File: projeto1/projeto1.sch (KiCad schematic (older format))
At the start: 17 parts

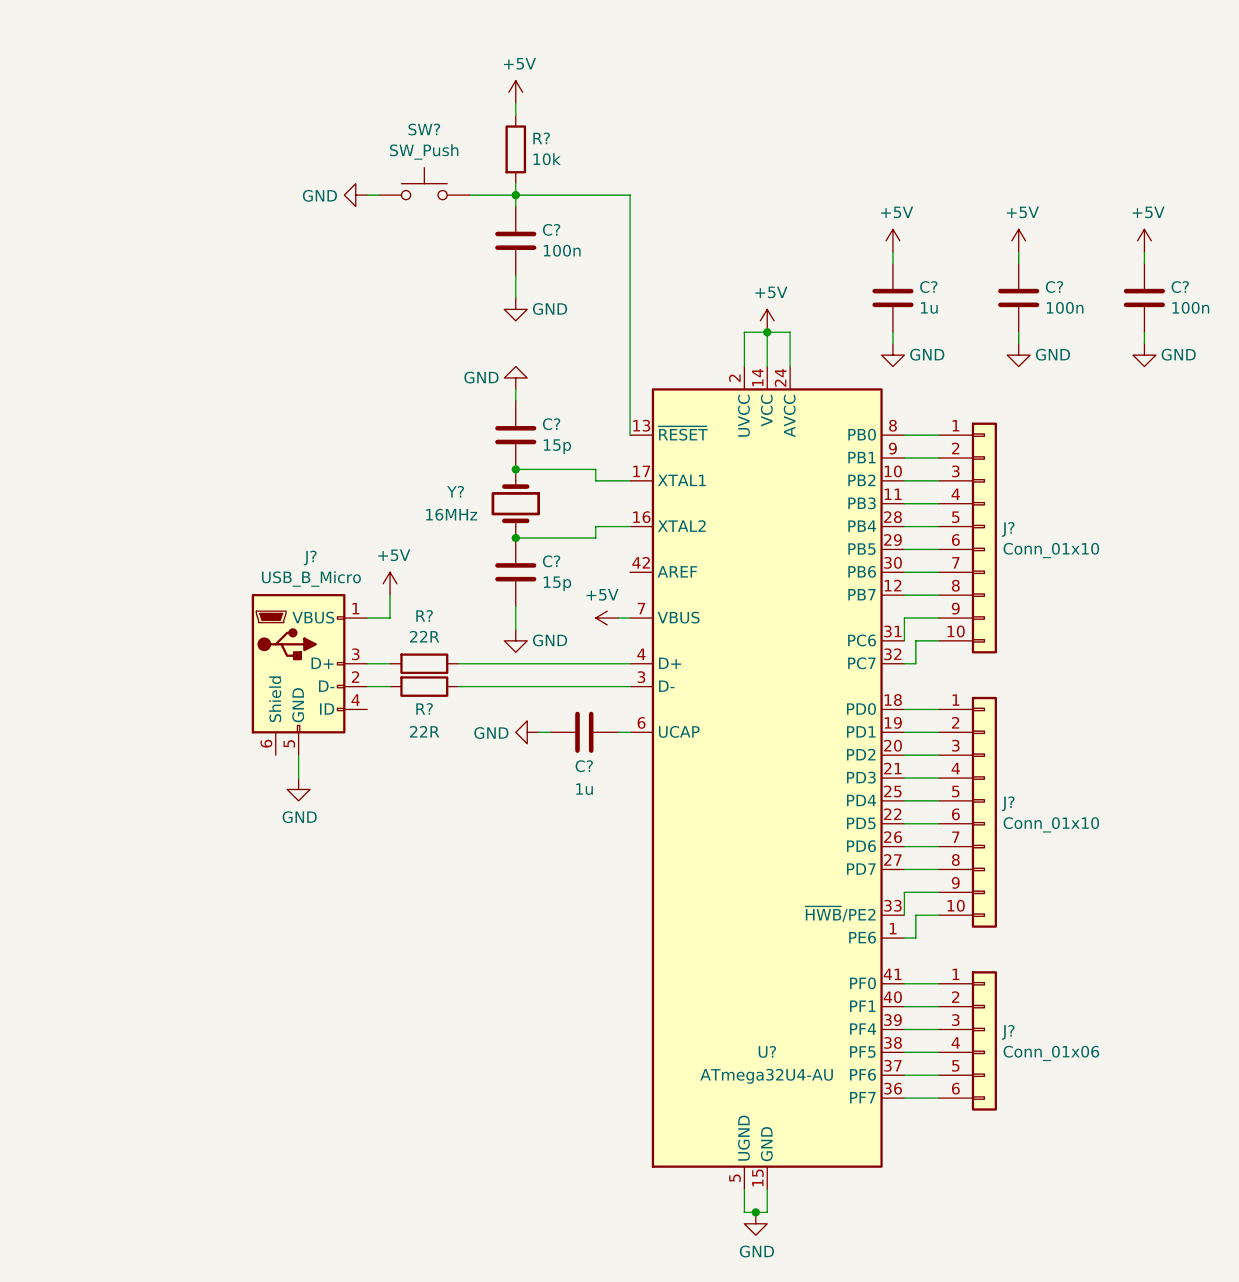
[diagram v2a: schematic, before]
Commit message: Identificadores adicionados
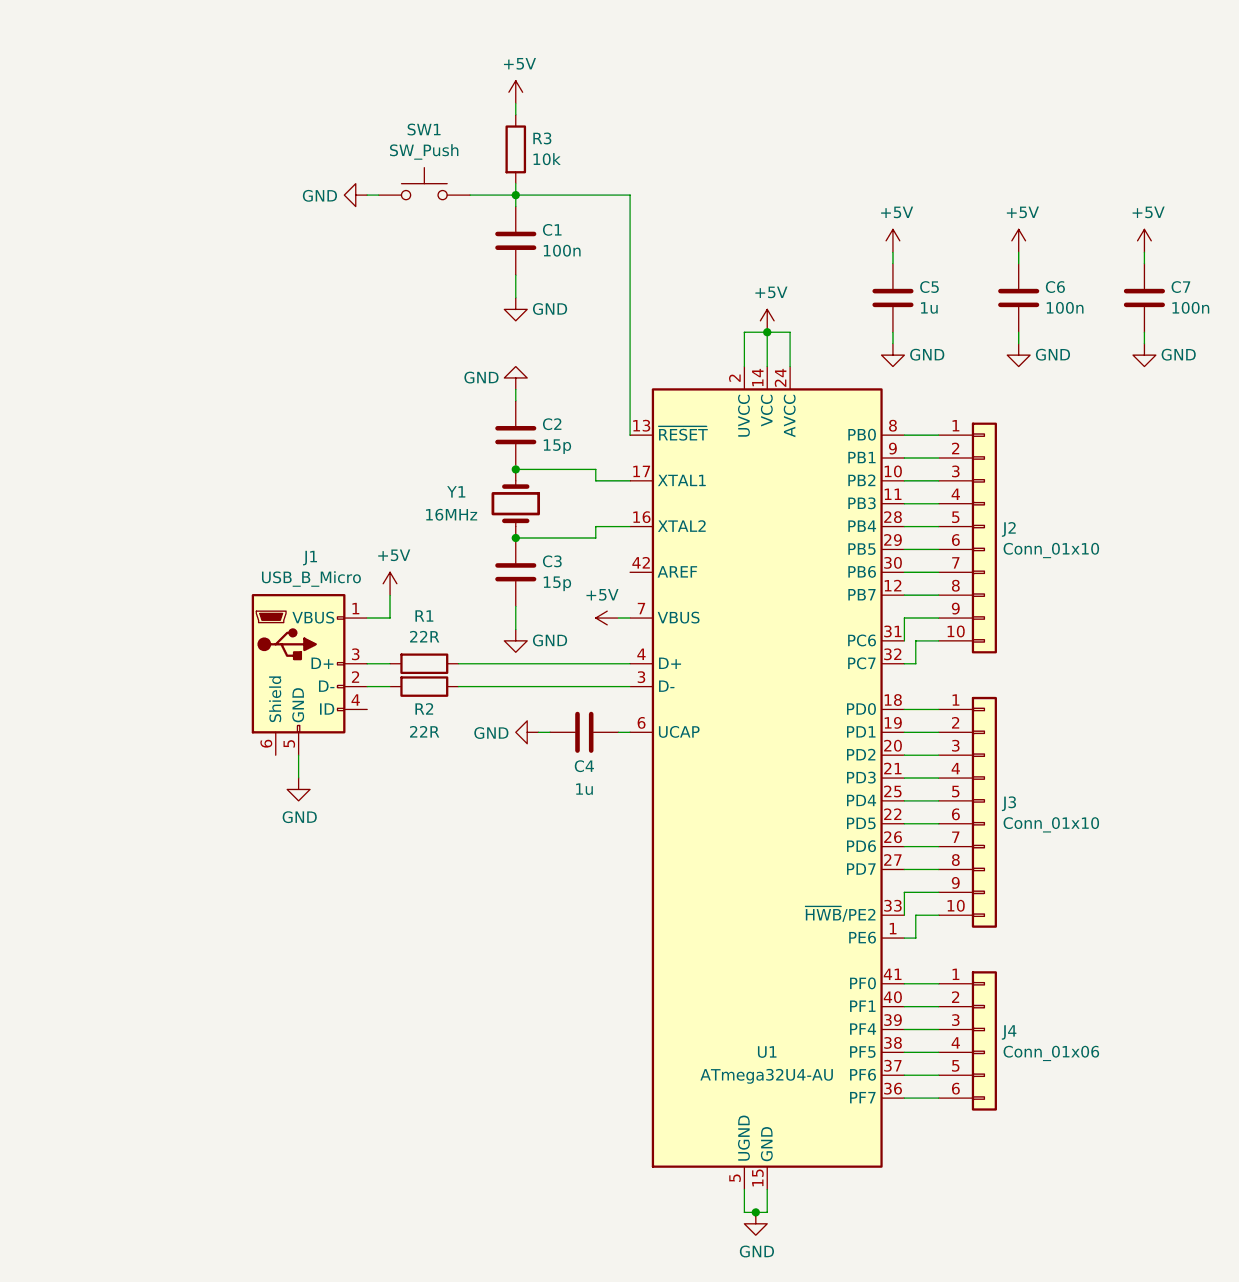
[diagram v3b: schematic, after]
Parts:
- gave numbers to parts that had none: 17
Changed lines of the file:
@@
 $EndDescr
 $Comp
-L Connector:USB_B_Micro J?
+L Connector:USB_B_Micro J1
 U 1 1 5D7A3DE3
 P 3500 3600
-F 0 "J?" H 3555 4067 50  0000 C CNN
+F 0 "J1" H 3555 4067 50  0000 C CNN
 F 1 "USB_B_Micro" H 3555 3976 50  0000 C CNN
 F 2 "" H 3650 3550 50  0001 C CNN
@@
 $EndComp
 $Comp
-L power:+5V #PWR?
+L power:+5V #PWR03
 U 1 1 5D7A3EE1
 P 3900 3300
-F 0 "#PWR?" H 3900 3150 50  0001 C CNN
+F 0 "#PWR03" H 3900 3150 50  0001 C CNN
 F 1 "+5V" H 3915 3473 50  0000 C CNN
 F 2 "" H 3900 3300 50  0001 C CNN
@@
 $EndComp
 $Comp
-L Device:R R?
+L Device:R R1
 U 1 1 5D7A400D
 P 4050 3600
-F 0 "R?" V 3843 3600 50  0000 C CNN
+F 0 "R1" V 3843 3600 50  0000 C CNN
 F 1 "22R" V 3934 3600 50  0000 C CNN
 F 2 "" V 3980 3600 50  0001 C CNN
@@
 $EndComp
 $Comp
-L Device:R R?
+L Device:R R2
 U 1 1 5D7A4271
 P 4050 3700
-F 0 "R?" V 4150 3700 50  0000 C CNN
+F 0 "R2" V 4150 3700 50  0000 C CNN
 F 1 "22R" V 4250 3700 50  0000 C CNN
 F 2 "" V 3980 3700 50  0001 C CNN
@@
 	3800 3700 3900 3700
 $Comp
-L power:GND #PWR?
+L power:GND #PWR01
 U 1 1 5D7A4CB3
 P 3500 4100
-F 0 "#PWR?" H 3500 3850 50  0001 C CNN
+F 0 "#PWR01" H 3500 3850 50  0001 C CNN
 F 1 "GND" H 3505 3927 50  0000 C CNN
 F 2 "" H 3500 4100 50  0001 C CNN
@@
 	3500 4100 3500 4000
 $Comp
-L power:+5V #PWR?
+L power:+5V #PWR011
 U 1 1 5D7A4E99
 P 5550 2150
-F 0 "#PWR?" H 5550 2000 50  0001 C CNN
+F 0 "#PWR011" H 5550 2000 50  0001 C CNN
 F 1 "+5V" H 5565 2323 50  0000 C CNN
 F 2 "" H 5550 2150 50  0001 C CNN
@@
 	5650 2150 5550 2150
 $Comp
-L power:GND #PWR?
+L power:GND #PWR010
 U 1 1 5D7A4FE0
 P 5500 6000
-F 0 "#PWR?" H 5500 5750 50  0001 C CNN
+F 0 "#PWR010" H 5500 5750 50  0001 C CNN
 F 1 "GND" H 5505 5827 50  0000 C CNN
 F 2 "" H 5500 6000 50  0001 C CNN
@@
 Connection ~ 5500 6000
 $Comp
-L Device:Crystal Y?
+L Device:Crystal Y1
 U 1 1 5D7A541D
 P 4450 2900
-F 0 "Y?" V 4400 2600 50  0000 L CNN
+F 0 "Y1" V 4400 2600 50  0000 L CNN
 F 1 "16MHz" V 4500 2500 50  0000 L CNN
 F 2 "" H 4450 2900 50  0001 C CNN
@@
 	4800 3000 4800 3050
 $Comp
-L Device:C C?
+L Device:C C2
 U 1 1 5D7A593F
 P 4450 2600
-F 0 "C?" H 4565 2646 50  0000 L CNN
+F 0 "C2" H 4565 2646 50  0000 L CNN
 F 1 "15p" H 4565 2555 50  0000 L CNN
 F 2 "" H 4488 2450 50  0001 C CNN
@@
 Connection ~ 4450 2750
 $Comp
-L Device:C C?
+L Device:C C3
 U 1 1 5D7A5A15
 P 4450 3200
-F 0 "C?" H 4565 3246 50  0000 L CNN
+F 0 "C3" H 4565 3246 50  0000 L CNN
 F 1 "15p" H 4565 3155 50  0000 L CNN
 F 2 "" H 4488 3050 50  0001 C CNN
@@
 Connection ~ 4450 3050
 $Comp
-L power:GND #PWR?
+L power:GND #PWR07
 U 1 1 5D7A6141
 P 4450 3450
-F 0 "#PWR?" H 4450 3200 50  0001 C CNN
+F 0 "#PWR07" H 4450 3200 50  0001 C CNN
 F 1 "GND" H 4600 3400 50  0000 C CNN
 F 2 "" H 4450 3450 50  0001 C CNN
@@
 	4450 2750 4800 2750
 $Comp
-L power:+5V #PWR?
+L power:+5V #PWR09
 U 1 1 5D7A8579
 P 4900 3400
-F 0 "#PWR?" H 4900 3250 50  0001 C CNN
+F 0 "#PWR09" H 4900 3250 50  0001 C CNN
 F 1 "+5V" V 5000 3400 50  0000 L CNN
 F 2 "" H 4900 3400 50  0001 C CNN
@@
 	4950 3400 4900 3400
 $Comp
-L Device:C C?
+L Device:C C4
 U 1 1 5D7A88D1
 P 4750 3900
-F 0 "C?" V 4900 3900 50  0000 C CNN
+F 0 "C4" V 4900 3900 50  0000 C CNN
 F 1 "1u" V 5000 3900 50  0000 C CNN
 F 2 "" H 4788 3750 50  0001 C CNN
@@
 	4950 3900 4900 3900
 $Comp
-L power:GND #PWR?
+L power:GND #PWR08
 U 1 1 5D7A8BF8
 P 4550 3900
-F 0 "#PWR?" H 4550 3650 50  0001 C CNN
+F 0 "#PWR08" H 4550 3650 50  0001 C CNN
 F 1 "GND" V 4555 3772 50  0000 R CNN
 F 2 "" H 4550 3900 50  0001 C CNN
@@
 	4600 3900 4550 3900
 $Comp
-L Device:C C?
+L Device:C C5
 U 1 1 5D7A8FE1
 P 6100 2000
-F 0 "C?" H 6215 2046 50  0000 L CNN
+F 0 "C5" H 6215 2046 50  0000 L CNN
 F 1 "1u" H 6215 1955 50  0000 L CNN
 F 2 "" H 6138 1850 50  0001 C CNN
@@
 $EndComp
 $Comp
-L Device:C C?
+L Device:C C6
 U 1 1 5D7A9043
 P 6650 2000
-F 0 "C?" H 6765 2046 50  0000 L CNN
+F 0 "C6" H 6765 2046 50  0000 L CNN
 F 1 "100n" H 6765 1955 50  0000 L CNN
 F 2 "" H 6688 1850 50  0001 C CNN
@@
 $EndComp
 $Comp
-L Device:C C?
+L Device:C C7
 U 1 1 5D7A9089
 P 7200 2000
-F 0 "C?" H 7315 2046 50  0000 L CNN
+F 0 "C7" H 7315 2046 50  0000 L CNN
 F 1 "100n" H 7315 1955 50  0000 L CNN
 F 2 "" H 7238 1850 50  0001 C CNN
@@
 $EndComp
 $Comp
-L power:+5V #PWR?
+L power:+5V #PWR012
 U 1 1 5D7A90CD
 P 6100 1800
-F 0 "#PWR?" H 6100 1650 50  0001 C CNN
+F 0 "#PWR012" H 6100 1650 50  0001 C CNN
 F 1 "+5V" H 6115 1973 50  0000 C CNN
 F 2 "" H 6100 1800 50  0001 C CNN
@@
 $EndComp
 $Comp
-L power:+5V #PWR?
+L power:+5V #PWR014
 U 1 1 5D7A90EE
 P 6650 1800
-F 0 "#PWR?" H 6650 1650 50  0001 C CNN
+F 0 "#PWR014" H 6650 1650 50  0001 C CNN
 F 1 "+5V" H 6665 1973 50  0000 C CNN
 F 2 "" H 6650 1800 50  0001 C CNN
@@
 $EndComp
 $Comp
-L power:+5V #PWR?
+L power:+5V #PWR016
 U 1 1 5D7A910F
 P 7200 1800
-F 0 "#PWR?" H 7200 1650 50  0001 C CNN
+F 0 "#PWR016" H 7200 1650 50  0001 C CNN
 F 1 "+5V" H 7215 1973 50  0000 C CNN
 F 2 "" H 7200 1800 50  0001 C CNN
@@
 $EndComp
 $Comp
-L power:GND #PWR?
+L power:GND #PWR06
 U 1 1 5D7A913B
 P 4450 2400
-F 0 "#PWR?" H 4450 2150 50  0001 C CNN
+F 0 "#PWR06" H 4450 2150 50  0001 C CNN
 F 1 "GND" H 4600 2350 50  0000 C CNN
 F 2 "" H 4450 2400 50  0001 C CNN
@@
 	4450 2400 4450 2450
 $Comp
-L power:GND #PWR?
+L power:GND #PWR013
 U 1 1 5D7A9871
 P 6100 2200
-F 0 "#PWR?" H 6100 1950 50  0001 C CNN
+F 0 "#PWR013" H 6100 1950 50  0001 C CNN
 F 1 "GND" H 6250 2150 50  0000 C CNN
 F 2 "" H 6100 2200 50  0001 C CNN
@@
 $EndComp
 $Comp
-L power:GND #PWR?
+L power:GND #PWR015
 U 1 1 5D7A98DE
 P 6650 2200
-F 0 "#PWR?" H 6650 1950 50  0001 C CNN
+F 0 "#PWR015" H 6650 1950 50  0001 C CNN
 F 1 "GND" H 6800 2150 50  0000 C CNN
 F 2 "" H 6650 2200 50  0001 C CNN
@@
 $EndComp
 $Comp
-L power:GND #PWR?
+L power:GND #PWR017
 U 1 1 5D7A98FF
 P 7200 2200
-F 0 "#PWR?" H 7200 1950 50  0001 C CNN
+F 0 "#PWR017" H 7200 1950 50  0001 C CNN
 F 1 "GND" H 7350 2150 50  0000 C CNN
 F 2 "" H 7200 2200 50  0001 C CNN
@@
 	7200 1850 7200 1800
 $Comp
-L Switch:SW_Push SW?
+L Switch:SW_Push SW1
 U 1 1 5D7AB198
 P 4050 1550
-F 0 "SW?" H 4050 1835 50  0000 C CNN
+F 0 "SW1" H 4050 1835 50  0000 C CNN
 F 1 "SW_Push" H 4050 1744 50  0000 C CNN
 F 2 "" H 4050 1750 50  0001 C CNN
@@
 $EndComp
 $Comp
-L Device:R R?
+L Device:R R3
 U 1 1 5D7ABA4B
 P 4450 1350
-F 0 "R?" H 4520 1396 50  0000 L CNN
+F 0 "R3" H 4520 1396 50  0000 L CNN
 F 1 "10k" H 4520 1305 50  0000 L CNN
 F 2 "" V 4380 1350 50  0001 C CNN
@@
 $EndComp
 $Comp
-L power:+5V #PWR?
+L power:+5V #PWR04
 U 1 1 5D7ABAF2
 P 4450 1150
-F 0 "#PWR?" H 4450 1000 50  0001 C CNN
+F 0 "#PWR04" H 4450 1000 50  0001 C CNN
 F 1 "+5V" H 4465 1323 50  0000 C CNN
 F 2 "" H 4450 1150 50  0001 C CNN
@@
 	4450 1200 4450 1150
 $Comp
-L power:GND #PWR?
+L power:GND #PWR02
 U 1 1 5D7ABFEF
 P 3800 1550
-F 0 "#PWR?" H 3800 1300 50  0001 C CNN
+F 0 "#PWR02" H 3800 1300 50  0001 C CNN
 F 1 "GND" V 3805 1422 50  0000 R CNN
 F 2 "" H 3800 1550 50  0001 C CNN
@@
 	3850 1550 3800 1550
 $Comp
-L Device:C C?
+L Device:C C1
 U 1 1 5D7AC572
 P 4450 1750
-F 0 "C?" H 4565 1796 50  0000 L CNN
+F 0 "C1" H 4565 1796 50  0000 L CNN
 F 1 "100n" H 4565 1705 50  0000 L CNN
 F 2 "" H 4488 1600 50  0001 C CNN
@@
 	4450 1500 4450 1550
 $Comp
-L power:GND #PWR?
+L power:GND #PWR05
 U 1 1 5D7AE3F3
 P 4450 2000
-F 0 "#PWR?" H 4450 1750 50  0001 C CNN
+F 0 "#PWR05" H 4450 1750 50  0001 C CNN
 F 1 "GND" H 4600 1950 50  0000 C CNN
 F 2 "" H 4450 2000 50  0001 C CNN
@@
 $EndComp
 $Comp
-L MCU_Microchip_ATmega:ATmega32U4-AU U?
+L MCU_Microchip_ATmega:ATmega32U4-AU U1
 U 1 1 5D7A3B59
 P 5550 4100
-F 0 "U?" H 5550 2900 50  0000 C CNN
+F 0 "U1" H 5550 2900 50  0000 C CNN
 F 1 "ATmega32U4-AU" H 5550 2800 50  0000 C CNN
 F 2 "Package_QFP:TQFP-44_10x10mm_P0.8mm" H 5550 4100 50  0001 C CIN
@@
 	4450 1900 4450 2000
 $Comp
-L Connector_Generic:Conn_01x10 J?
+L Connector_Generic:Conn_01x10 J2
 U 1 1 5D7B5850
 P 6500 3000
-F 0 "J?" H 6580 2992 50  0000 L CNN
+F 0 "J2" H 6580 2992 50  0000 L CNN
 F 1 "Conn_01x10" H 6580 2901 50  0000 L CNN
 F 2 "" H 6500 3000 50  0001 C CNN
@@
 	6200 3600 6150 3600
 $Comp
-L Connector_Generic:Conn_01x10 J?
+L Connector_Generic:Conn_01x10 J3
 U 1 1 5D7BB060
 P 6500 4200
-F 0 "J?" H 6580 4192 50  0000 L CNN
+F 0 "J3" H 6580 4192 50  0000 L CNN
 F 1 "Conn_01x10" H 6580 4101 50  0000 L CNN
 F 2 "" H 6500 4200 50  0001 C CNN
@@
 	6200 4800 6150 4800
 $Comp
-L Connector_Generic:Conn_01x06 J?
+L Connector_Generic:Conn_01x06 J4
 U 1 1 5D7C54FC
 P 6500 5200
-F 0 "J?" H 6580 5192 50  0000 L CNN
+F 0 "J4" H 6580 5192 50  0000 L CNN
 F 1 "Conn_01x06" H 6580 5101 50  0000 L CNN
 F 2 "" H 6500 5200 50  0001 C CNN

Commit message: Footprints atribuidas
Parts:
- C1, C2, C3, C4, C5, C6, C7: footprint (none) -> Capacitor_SMD:C_0805_2012Metric_Pad1.15x1.40mm_HandSolder
- J1: footprint (none) -> Connector_USB:USB_Mini-B_AdamTech_MUSB-B5-S-VT-TSMT-1_SMD_Vertical
- J2, J3: footprint (none) -> Connector_PinHeader_2.54mm:PinHeader_1x10_P2.54mm_Vertical
- J4: footprint (none) -> Connector_PinHeader_2.54mm:PinHeader_1x06_P2.54mm_Vertical
- R1, R2, R3: footprint (none) -> Resistor_SMD:R_1206_3216Metric_Pad1.42x1.75mm_HandSolder
- SW1: footprint (none) -> Button_Switch_THT:SW_PUSH_6mm
- Y1: footprint (none) -> Crystal:Crystal_SMD_5032-2Pin_5.0x3.2mm_HandSoldering
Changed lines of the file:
@@
 F 0 "J1" H 3555 4067 50  0000 C CNN
 F 1 "USB_B_Micro" H 3555 3976 50  0000 C CNN
-F 2 "" H 3650 3550 50  0001 C CNN
+F 2 "Connector_USB:USB_Mini-B_AdamTech_MUSB-B5-S-VT-TSMT-1_SMD_Vertical" H 3650 3550 50  0001 C CNN
 F 3 "~" H 3650 3550 50  0001 C CNN
 	1    3500 3600
@@
 F 0 "R1" V 3843 3600 50  0000 C CNN
 F 1 "22R" V 3934 3600 50  0000 C CNN
-F 2 "" V 3980 3600 50  0001 C CNN
+F 2 "Resistor_SMD:R_1206_3216Metric_Pad1.42x1.75mm_HandSolder" V 3980 3600 50  0001 C CNN
 F 3 "~" H 4050 3600 50  0001 C CNN
 	1    4050 3600
@@
 F 0 "R2" V 4150 3700 50  0000 C CNN
 F 1 "22R" V 4250 3700 50  0000 C CNN
-F 2 "" V 3980 3700 50  0001 C CNN
+F 2 "Resistor_SMD:R_1206_3216Metric_Pad1.42x1.75mm_HandSolder" V 3980 3700 50  0001 C CNN
 F 3 "~" H 4050 3700 50  0001 C CNN
 	1    4050 3700
@@
 	5550 6000 5500 6000
 Connection ~ 5500 6000
-$Comp
-L Device:Crystal Y1
-U 1 1 5D7A541D
-P 4450 2900
-F 0 "Y1" V 4400 2600 50  0000 L CNN
-F 1 "16MHz" V 4500 2500 50  0000 L CNN
-F 2 "" H 4450 2900 50  0001 C CNN
-F 3 "~" H 4450 2900 50  0001 C CNN
-	1    4450 2900
-	0    1    1    0
-$EndComp
 Wire Wire Line
 	4950 2800 4800 2800
@@
 F 0 "C2" H 4565 2646 50  0000 L CNN
 F 1 "15p" H 4565 2555 50  0000 L CNN
-F 2 "" H 4488 2450 50  0001 C CNN
+F 2 "Capacitor_SMD:C_0805_2012Metric_Pad1.15x1.40mm_HandSolder" H 4488 2450 50  0001 C CNN
 F 3 "~" H 4450 2600 50  0001 C CNN
 	1    4450 2600
 	1    0    0    -1
 $EndComp
-Connection ~ 4450 2750
 $Comp
 L Device:C C3
@@
 F 0 "C3" H 4565 3246 50  0000 L CNN
 F 1 "15p" H 4565 3155 50  0000 L CNN
-F 2 "" H 4488 3050 50  0001 C CNN
+F 2 "Capacitor_SMD:C_0805_2012Metric_Pad1.15x1.40mm_HandSolder" H 4488 3050 50  0001 C CNN
 F 3 "~" H 4450 3200 50  0001 C CNN
 	1    4450 3200
 	1    0    0    -1
 $EndComp
-Connection ~ 4450 3050
 $Comp
 L power:GND #PWR07
@@
 F 0 "C4" V 4900 3900 50  0000 C CNN
 F 1 "1u" V 5000 3900 50  0000 C CNN
-F 2 "" H 4788 3750 50  0001 C CNN
+F 2 "Capacitor_SMD:C_0805_2012Metric_Pad1.15x1.40mm_HandSolder" H 4788 3750 50  0001 C CNN
 F 3 "~" H 4750 3900 50  0001 C CNN
 	1    4750 3900
@@
 F 0 "C5" H 6215 2046 50  0000 L CNN
 F 1 "1u" H 6215 1955 50  0000 L CNN
-F 2 "" H 6138 1850 50  0001 C CNN
+F 2 "Capacitor_SMD:C_0805_2012Metric_Pad1.15x1.40mm_HandSolder" H 6138 1850 50  0001 C CNN
 F 3 "~" H 6100 2000 50  0001 C CNN
 	1    6100 2000
@@
 F 0 "C6" H 6765 2046 50  0000 L CNN
 F 1 "100n" H 6765 1955 50  0000 L CNN
-F 2 "" H 6688 1850 50  0001 C CNN
+F 2 "Capacitor_SMD:C_0805_2012Metric_Pad1.15x1.40mm_HandSolder" H 6688 1850 50  0001 C CNN
 F 3 "~" H 6650 2000 50  0001 C CNN
 	1    6650 2000
@@
 F 0 "C7" H 7315 2046 50  0000 L CNN
 F 1 "100n" H 7315 1955 50  0000 L CNN
-F 2 "" H 7238 1850 50  0001 C CNN
+F 2 "Capacitor_SMD:C_0805_2012Metric_Pad1.15x1.40mm_HandSolder" H 7238 1850 50  0001 C CNN
 F 3 "~" H 7200 2000 50  0001 C CNN
 	1    7200 2000
@@
 F 0 "SW1" H 4050 1835 50  0000 C CNN
 F 1 "SW_Push" H 4050 1744 50  0000 C CNN
-F 2 "" H 4050 1750 50  0001 C CNN
+F 2 "Button_Switch_THT:SW_PUSH_6mm" H 4050 1750 50  0001 C CNN
 F 3 "" H 4050 1750 50  0001 C CNN
 	1    4050 1550
@@
 F 0 "R3" H 4520 1396 50  0000 L CNN
 F 1 "10k" H 4520 1305 50  0000 L CNN
-F 2 "" V 4380 1350 50  0001 C CNN
+F 2 "Resistor_SMD:R_1206_3216Metric_Pad1.42x1.75mm_HandSolder" V 4380 1350 50  0001 C CNN
 F 3 "~" H 4450 1350 50  0001 C CNN
 	1    4450 1350
@@
 F 0 "C1" H 4565 1796 50  0000 L CNN
 F 1 "100n" H 4565 1705 50  0000 L CNN
-F 2 "" H 4488 1600 50  0001 C CNN
+F 2 "Capacitor_SMD:C_0805_2012Metric_Pad1.15x1.40mm_HandSolder" H 4488 1600 50  0001 C CNN
 F 3 "~" H 4450 1750 50  0001 C CNN
 	1    4450 1750
@@
 F 0 "J2" H 6580 2992 50  0000 L CNN
 F 1 "Conn_01x10" H 6580 2901 50  0000 L CNN
-F 2 "" H 6500 3000 50  0001 C CNN
+F 2 "Connector_PinHeader_2.54mm:PinHeader_1x10_P2.54mm_Vertical" H 6500 3000 50  0001 C CNN
 F 3 "~" H 6500 3000 50  0001 C CNN
 	1    6500 3000
@@
 F 0 "J3" H 6580 4192 50  0000 L CNN
 F 1 "Conn_01x10" H 6580 4101 50  0000 L CNN
-F 2 "" H 6500 4200 50  0001 C CNN
+F 2 "Connector_PinHeader_2.54mm:PinHeader_1x10_P2.54mm_Vertical" H 6500 4200 50  0001 C CNN
 F 3 "~" H 6500 4200 50  0001 C CNN
 	1    6500 4200
@@
 F 0 "J4" H 6580 5192 50  0000 L CNN
 F 1 "Conn_01x06" H 6580 5101 50  0000 L CNN
-F 2 "" H 6500 5200 50  0001 C CNN
+F 2 "Connector_PinHeader_2.54mm:PinHeader_1x06_P2.54mm_Vertical" H 6500 5200 50  0001 C CNN
 F 3 "~" H 6500 5200 50  0001 C CNN
 	1    6500 5200
@@
 Wire Wire Line
 	6300 5500 6150 5500
+Connection ~ 4450 3050
+Connection ~ 4450 2750
+$Comp
+L Device:Crystal Y1
+U 1 1 5D7A541D
+P 4450 2900
+F 0 "Y1" V 4400 2600 50  0000 L CNN
+F 1 "16MHz" V 4500 2500 50  0000 L CNN
+F 2 "Crystal:Crystal_SMD_5032-2Pin_5.0x3.2mm_HandSoldering" H 4450 2900 50  0001 C CNN
+F 3 "~" H 4450 2900 50  0001 C CNN
+	1    4450 2900
+	0    1    1    0
+$EndComp
 $EndSCHEMATC
